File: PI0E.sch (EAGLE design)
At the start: 36 parts, among them IC1 ENC28J60QFN, T1 WE-LAN-10/100/1000-BASE-T,749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, U1 TPS73533DRVR, U2 CAT24C32WI-GT3, X1 22-23-2021, X2 22-23-2021

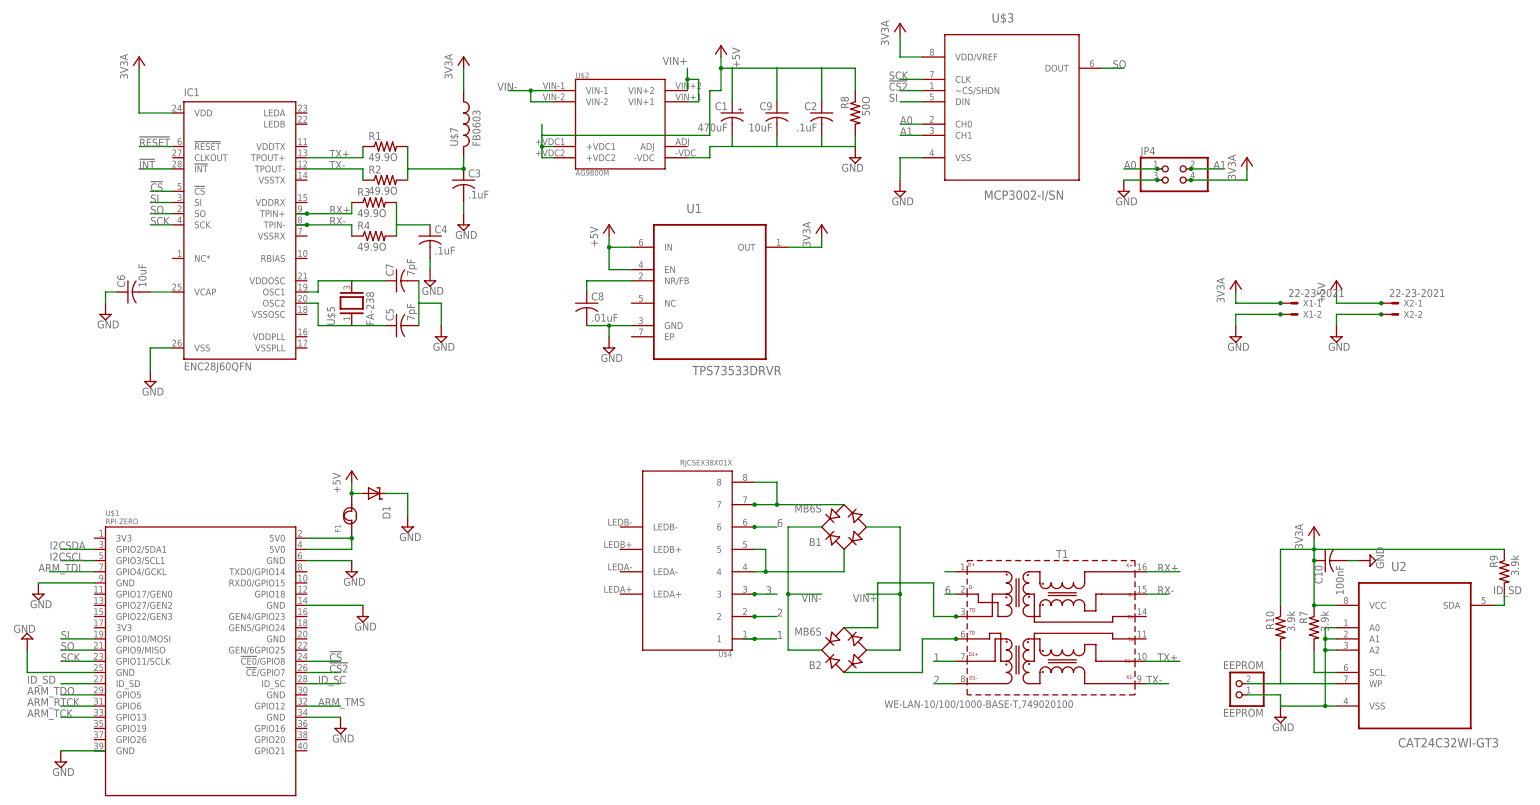
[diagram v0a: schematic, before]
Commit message: Cleaning up routing
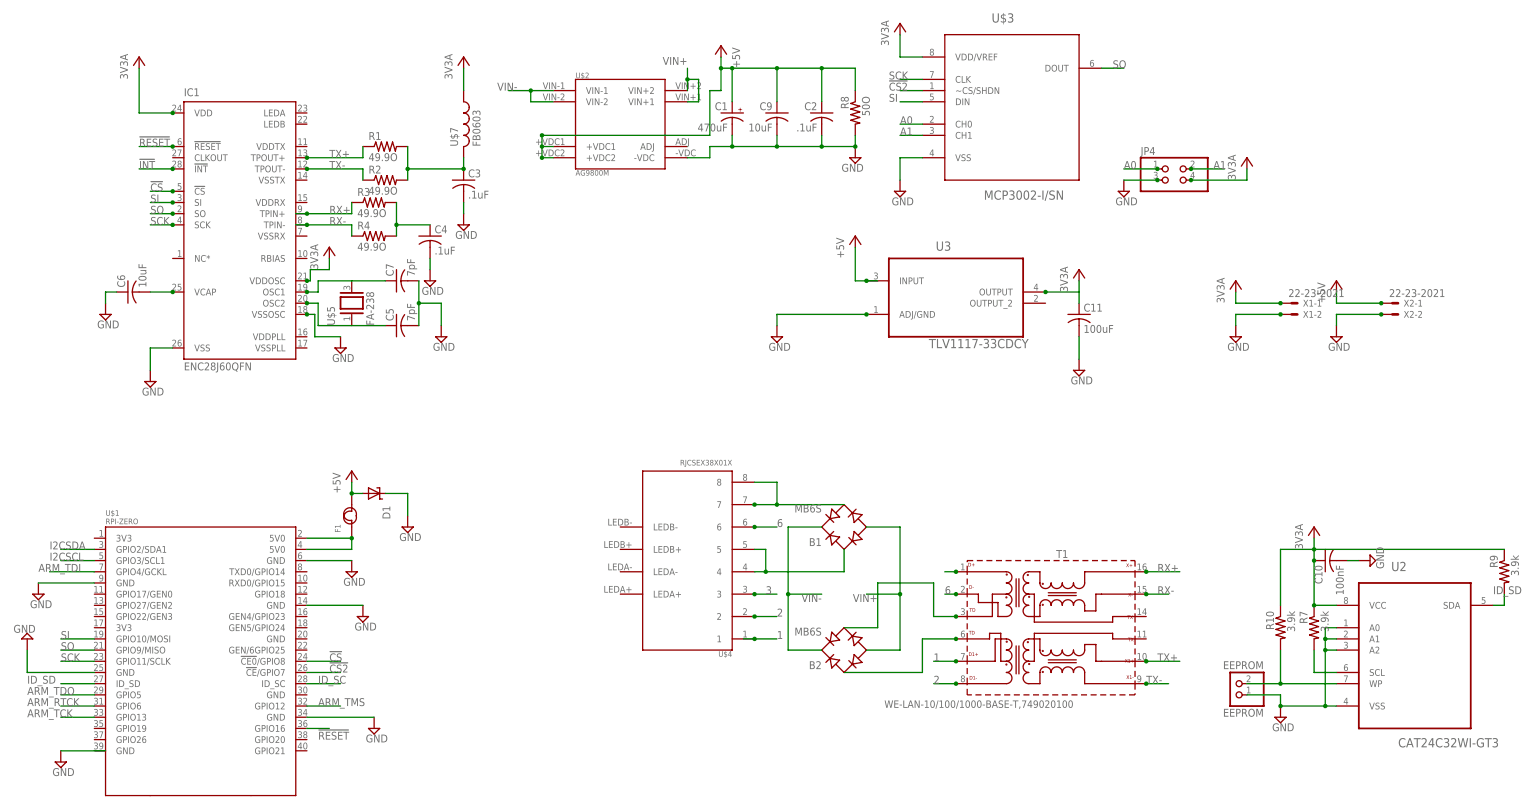
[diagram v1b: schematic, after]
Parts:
- removed C8: .01uF, rcl:C-USC0603
- removed U1: TPS73533DRVR, Texas Instruments_By_element14_Batch_1:TPS73533DRVR
- added C11: 100uF, rcl:C-USC0603
- added U3: TLV1117-33CDCY, Texas Instruments_By_element14_Batch_1:TLV1117-33CDCY
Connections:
- removed net N$20: C8.1, U1.NR/FB
- net !RESET: now also U$1.GPIO16
- net +3V3: now also C11.1, IC1.VDDOSC, U3.OUTPUT; no longer U1.OUT
- net +5V: now also U3.INPUT; no longer U1.EN, U1.IN
- net GND: now also C11.2, IC1.VSSOSC, U3.ADJ/GND; no longer C8.2, U1.GND

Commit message: copper pour for the 3.3v regulator. A few cleaned traces.
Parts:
- renumbered IC1 to ENC28J60, U$3 to MCP3002, U$5 to OSC, U$7 to FB, U2 to CAT24, U3 to TLV1137

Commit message: fixed missing RX line
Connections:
- net 3: now also T1.D+
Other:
- moved on the sheet: T1
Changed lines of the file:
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@@
 <instance part="R3" gate="G$1" x="88.9" y="154.94"/>
 <instance part="R4" gate="G$1" x="88.9" y="147.32"/>
-<instance part="T1" gate="G$1" x="243.84" y="58.42"/>
+<instance part="T1" gate="G$1" x="243.332" y="58.42"/>
 <instance part="3V3A3" gate="G$1" x="284.48" y="137.16"/>
 <instance part="SUPPLY10" gate="GND" x="284.48" y="124.46"/>
@@
 <segment>
 <pinref part="T1" gate="G$1" pin="D1-"/>
-<wire x1="220.98" y1="45.72" x2="215.9" y2="45.72" width="0.1524" layer="91"/>
+<wire x1="220.472" y1="45.72" x2="215.9" y2="45.72" width="0.1524" layer="91"/>
 <label x="215.9" y="45.72" size="1.778" layer="95"/>
-<junction x="220.98" y="45.72"/>
+<junction x="220.472" y="45.72"/>
 </segment>
 </net>
@@
 </segment>
 <segment>
-<wire x1="220.98" y1="71.12" x2="218.44" y2="71.12" width="0.1524" layer="91"/>
-<junction x="220.98" y="71.12"/>
+<wire x1="220.98" y1="71.12" x2="220.442" y2="71.12" width="0.1524" layer="91"/>
+<pinref part="T1" gate="G$1" pin="D+"/>
+<wire x1="220.442" y1="71.12" x2="215.9" y2="71.12" width="0.1524" layer="91"/>
+<junction x="220.442" y="71.12"/>
 </segment>
 </net>
@@
 <segment>
 <pinref part="T1" gate="G$1" pin="D-"/>
-<wire x1="220.98" y1="66.04" x2="218.44" y2="66.04" width="0.1524" layer="91"/>
+<wire x1="220.472" y1="66.04" x2="218.44" y2="66.04" width="0.1524" layer="91"/>
 <label x="218.44" y="66.04" size="1.778" layer="95"/>
-<junction x="220.98" y="66.04"/>
+<junction x="220.472" y="66.04"/>
 </segment>
 </net>
@@
 <wire x1="215.9" y1="68.58" x2="215.9" y2="60.96" width="0.1524" layer="91"/>
 <pinref part="T1" gate="G$1" pin="TD1"/>
-<wire x1="215.9" y1="60.96" x2="220.98" y2="60.96" width="0.1524" layer="91"/>
-<junction x="220.98" y="60.96"/>
+<wire x1="215.9" y1="60.96" x2="220.472" y2="60.96" width="0.1524" layer="91"/>
+<junction x="220.472" y="60.96"/>
 </segment>
 </net>
@@
 <wire x1="213.36" y1="48.26" x2="213.36" y2="55.88" width="0.1524" layer="91"/>
 <pinref part="T1" gate="G$1" pin="TD2"/>
-<wire x1="213.36" y1="55.88" x2="220.98" y2="55.88" width="0.1524" layer="91"/>
-<junction x="220.98" y="55.88"/>
+<wire x1="213.36" y1="55.88" x2="220.472" y2="55.88" width="0.1524" layer="91"/>
+<junction x="220.472" y="55.88"/>
 </segment>
 </net>
@@
 <segment>
 <pinref part="T1" gate="G$1" pin="X1+"/>
-<wire x1="264.16" y1="50.8" x2="269.24" y2="50.8" width="0.1524" layer="91"/>
-<wire x1="271.78" y1="50.8" x2="269.24" y2="50.8" width="0.1524" layer="91"/>
+<wire x1="263.652" y1="50.8" x2="271.78" y2="50.8" width="0.1524" layer="91"/>
 <label x="266.7" y="50.8" size="1.778" layer="95"/>
-<junction x="264.16" y="50.8"/>
+<junction x="263.652" y="50.8"/>
 </segment>
 </net>
@@
 <segment>
 <pinref part="T1" gate="G$1" pin="D1+"/>
-<wire x1="220.98" y1="50.8" x2="215.9" y2="50.8" width="0.1524" layer="91"/>
+<wire x1="220.472" y1="50.8" x2="215.9" y2="50.8" width="0.1524" layer="91"/>
 <label x="215.9" y="50.8" size="1.778" layer="95"/>
-<junction x="220.98" y="50.8"/>
+<junction x="220.472" y="50.8"/>
 </segment>
 </net>
@@
 <segment>
 <pinref part="T1" gate="G$1" pin="X1-"/>
-<wire x1="264.16" y1="45.72" x2="269.24" y2="45.72" width="0.1524" layer="91"/>
+<wire x1="263.652" y1="45.72" x2="269.24" y2="45.72" width="0.1524" layer="91"/>
 <label x="264.16" y="45.72" size="1.778" layer="95"/>
-<junction x="264.16" y="45.72"/>
+<junction x="263.652" y="45.72"/>
 </segment>
 </net>
@@
 <segment>
 <pinref part="T1" gate="G$1" pin="X+"/>
-<wire x1="264.16" y1="71.12" x2="271.78" y2="71.12" width="0.1524" layer="91"/>
+<wire x1="263.652" y1="71.12" x2="271.78" y2="71.12" width="0.1524" layer="91"/>
 <label x="266.7" y="71.12" size="1.778" layer="95"/>
-<junction x="264.16" y="71.12"/>
+<junction x="263.652" y="71.12"/>
 </segment>
 </net>
@@
 <segment>
 <pinref part="T1" gate="G$1" pin="X-"/>
-<wire x1="264.16" y1="66.04" x2="269.24" y2="66.04" width="0.1524" layer="91"/>
+<wire x1="263.652" y1="66.04" x2="269.24" y2="66.04" width="0.1524" layer="91"/>
 <label x="266.7" y="66.04" size="1.778" layer="95"/>
-<junction x="264.16" y="66.04"/>
-</segment>
-</net>
+<junction x="263.652" y="66.04"/>
+</segment>
+</net>

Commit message: fixed encj rx/tx power lines. and switch v+ v- pins into the poe module.
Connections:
- net +3V3: now also ENC28J60.VDDRX, ENC28J60.VDDTX
- net GND: now also ENC28J60.VSSRX, ENC28J60.VSSTX
- net VIN+: now also B1.+, B2.+; no longer B1.-, B2.-
- net VIN-: now also B1.-, B2.-; no longer B1.+, B2.+
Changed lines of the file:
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@@
 <?xml version="1.0" encoding="utf-8"?>
 <!DOCTYPE eagle SYSTEM "eagle.dtd">
-<eagle version="7.5.0">
+<eagle version="6.5.0">
 <drawing>
 <settings>
@@
 <part name="SUPPLY13" library="supply2" deviceset="GND" device=""/>
 <part name="SUPPLY4" library="supply2" deviceset="GND" device=""/>
+<part name="SUPPLY16" library="supply2" deviceset="GND" device=""/>
+<part name="SUPPLY24" library="supply2" deviceset="GND" device=""/>
+<part name="3V3A5" library="supply1" deviceset="+3V3" device="" value="3V3A"/>
+<part name="3V3A7" library="supply1" deviceset="+3V3" device="" value="3V3A"/>
 </parts>
 <sheets>
@@
 <instance part="SUPPLY13" gate="GND" x="248.92" y="116.84"/>
 <instance part="SUPPLY4" gate="GND" x="180.34" y="124.46"/>
+<instance part="SUPPLY16" gate="GND" x="82.042" y="144.78"/>
+<instance part="SUPPLY24" gate="GND" x="81.28" y="157.48"/>
+<instance part="3V3A5" gate="G$1" x="81.28" y="172.72"/>
+<instance part="3V3A7" gate="G$1" x="78.74" y="160.02"/>
 </instances>
 <busses>
@@
 <junction x="200.66" y="129.54"/>
 <pinref part="SUPPLY4" gate="GND" pin="GND"/>
+</segment>
+<segment>
+<pinref part="ENC28J60" gate="G$1" pin="VSSRX"/>
+<wire x1="73.66" y1="147.32" x2="82.042" y2="147.32" width="0.1524" layer="91"/>
+<pinref part="SUPPLY16" gate="GND" pin="GND"/>
+<wire x1="82.042" y1="147.32" x2="82.296" y2="147.32" width="0.1524" layer="91"/>
+<junction x="82.042" y="147.32"/>
+</segment>
+<segment>
+<pinref part="ENC28J60" gate="G$1" pin="VSSTX"/>
+<wire x1="73.66" y1="160.02" x2="81.28" y2="160.02" width="0.1524" layer="91"/>
+<pinref part="SUPPLY24" gate="GND" pin="GND"/>
 </segment>
 </net>
@@
 <net name="VIN-" class="0">
 <segment>
-<pinref part="B2" gate="G$1" pin="+"/>
-<wire x1="190.5" y1="53.34" x2="182.88" y2="53.34" width="0.1524" layer="91"/>
-<wire x1="182.88" y1="53.34" x2="182.88" y2="66.04" width="0.1524" layer="91"/>
-<pinref part="B1" gate="G$1" pin="+"/>
-<wire x1="182.88" y1="66.04" x2="182.88" y2="81.28" width="0.1524" layer="91"/>
-<wire x1="182.88" y1="81.28" x2="190.5" y2="81.28" width="0.1524" layer="91"/>
-<wire x1="182.88" y1="66.04" x2="190.5" y2="66.04" width="0.1524" layer="91"/>
-<junction x="182.88" y="66.04"/>
-<label x="190.5" y="66.04" size="1.778" layer="95" rot="R180"/>
-</segment>
-<segment>
 <wire x1="129.54" y1="180.34" x2="124.46" y2="180.34" width="0.1524" layer="91"/>
 <wire x1="124.46" y1="180.34" x2="124.46" y2="177.8" width="0.1524" layer="91"/>
@@
 <pinref part="U$2" gate="G$1" pin="VIN-2"/>
 </segment>
+<segment>
+<pinref part="B1" gate="G$1" pin="-"/>
+<wire x1="200.66" y1="81.28" x2="205.74" y2="81.28" width="0.1524" layer="91"/>
+<wire x1="205.74" y1="81.28" x2="205.74" y2="76.2" width="0.1524" layer="91"/>
+<pinref part="B2" gate="G$1" pin="-"/>
+<wire x1="205.74" y1="76.2" x2="205.74" y2="53.34" width="0.1524" layer="91"/>
+<wire x1="205.74" y1="53.34" x2="200.66" y2="53.34" width="0.1524" layer="91"/>
+<wire x1="205.74" y1="76.2" x2="210.82" y2="76.2" width="0.1524" layer="91"/>
+<junction x="205.74" y="76.2"/>
+<label x="205.74" y="76.2" size="1.778" layer="95"/>
+</segment>
 </net>
 <net name="VIN+" class="0">
-<segment>
-<pinref part="B2" gate="G$1" pin="-"/>
-<wire x1="200.66" y1="53.34" x2="208.28" y2="53.34" width="0.1524" layer="91"/>
-<wire x1="208.28" y1="53.34" x2="208.28" y2="66.04" width="0.1524" layer="91"/>
-<pinref part="B1" gate="G$1" pin="-"/>
-<wire x1="208.28" y1="66.04" x2="208.28" y2="81.28" width="0.1524" layer="91"/>
-<wire x1="208.28" y1="81.28" x2="200.66" y2="81.28" width="0.1524" layer="91"/>
-<wire x1="208.28" y1="66.04" x2="200.66" y2="66.04" width="0.1524" layer="91"/>
-<label x="203.2" y="66.04" size="1.778" layer="95" rot="R180"/>
-<junction x="208.28" y="66.04"/>
-</segment>
 <segment>
 <label x="160.02" y="187.96" size="1.778" layer="95" rot="R180"/>
@@
 <pinref part="U$2" gate="G$1" pin="VIN+1"/>
 <pinref part="U$2" gate="G$1" pin="VIN+2"/>
+</segment>
+<segment>
+<pinref part="B1" gate="G$1" pin="+"/>
+<wire x1="190.5" y1="81.28" x2="185.42" y2="81.28" width="0.1524" layer="91"/>
+<wire x1="185.42" y1="81.28" x2="185.42" y2="66.04" width="0.1524" layer="91"/>
+<pinref part="B2" gate="G$1" pin="+"/>
+<wire x1="185.42" y1="66.04" x2="185.42" y2="53.34" width="0.1524" layer="91"/>
+<wire x1="185.42" y1="53.34" x2="190.5" y2="53.34" width="0.1524" layer="91"/>
+<wire x1="185.42" y1="66.04" x2="190.5" y2="66.04" width="0.1524" layer="91"/>
+<junction x="185.42" y="66.04"/>
+<label x="185.42" y="66.04" size="1.778" layer="95"/>
 </segment>
 </net>
@@
 <junction x="73.66" y="137.16"/>
 </segment>
-</net>
+<segment>
+<pinref part="ENC28J60" gate="G$1" pin="VDDTX"/>
+<wire x1="73.66" y1="167.64" x2="81.28" y2="167.64" width="0.1524" layer="91"/>
+<wire x1="81.28" y1="167.64" x2="81.28" y2="170.18" width="0.1524" layer="91"/>
+<pinref part="3V3A5" gate="G$1" pin="+3V3"/>
+</segment>
+<segment>
+<pinref part="ENC28J60" gate="G$1" pin="VDDRX"/>
+<wire x1="73.66" y1="154.94" x2="78.74" y2="154.94" width="0.1524" layer="91"/>
+<wire x1="78.74" y1="154.94" x2="78.74" y2="157.48" width="0.1524" layer="91"/>
+<pinref part="3V3A7" gate="G$1" pin="+3V3"/>
+</segment>
+</net>
